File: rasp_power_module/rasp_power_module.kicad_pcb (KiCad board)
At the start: 2 copper layers, 45.7 x 59.3 mm, 22 parts, among them J1 Conn_01x02, J2 Conn_01x05, J3 Conn_01x02, J5 Conn_01x02, J7 Conn_01x02, J8 Conn_01x02, J9 Conn_01x02, K1 G5V-1, K2 SANYOU_SRD_Form_C, Q1 S8050 J3Y

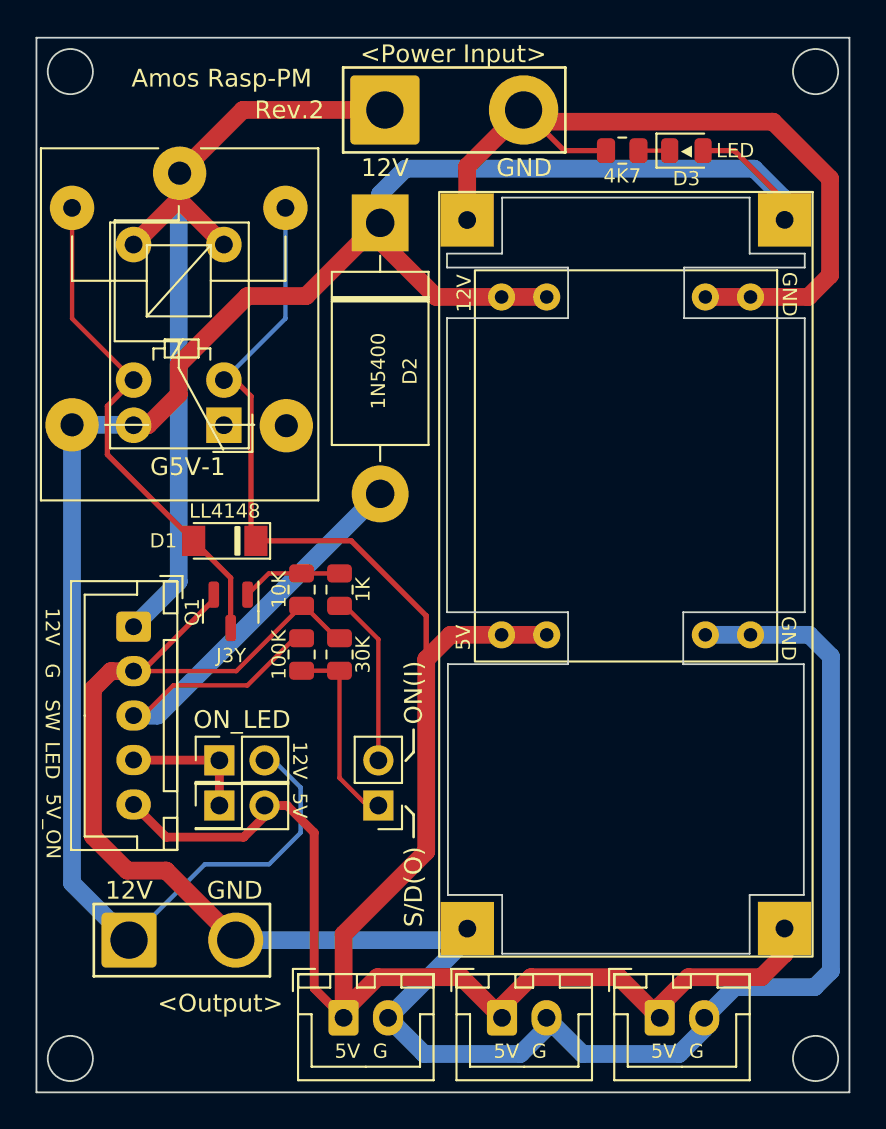
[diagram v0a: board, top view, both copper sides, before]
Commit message: rev.3  - mp1584 보드 핀아웃 조정
Signed-off-by: Ju, Gyeong-min <jcmh74@gmail.com>
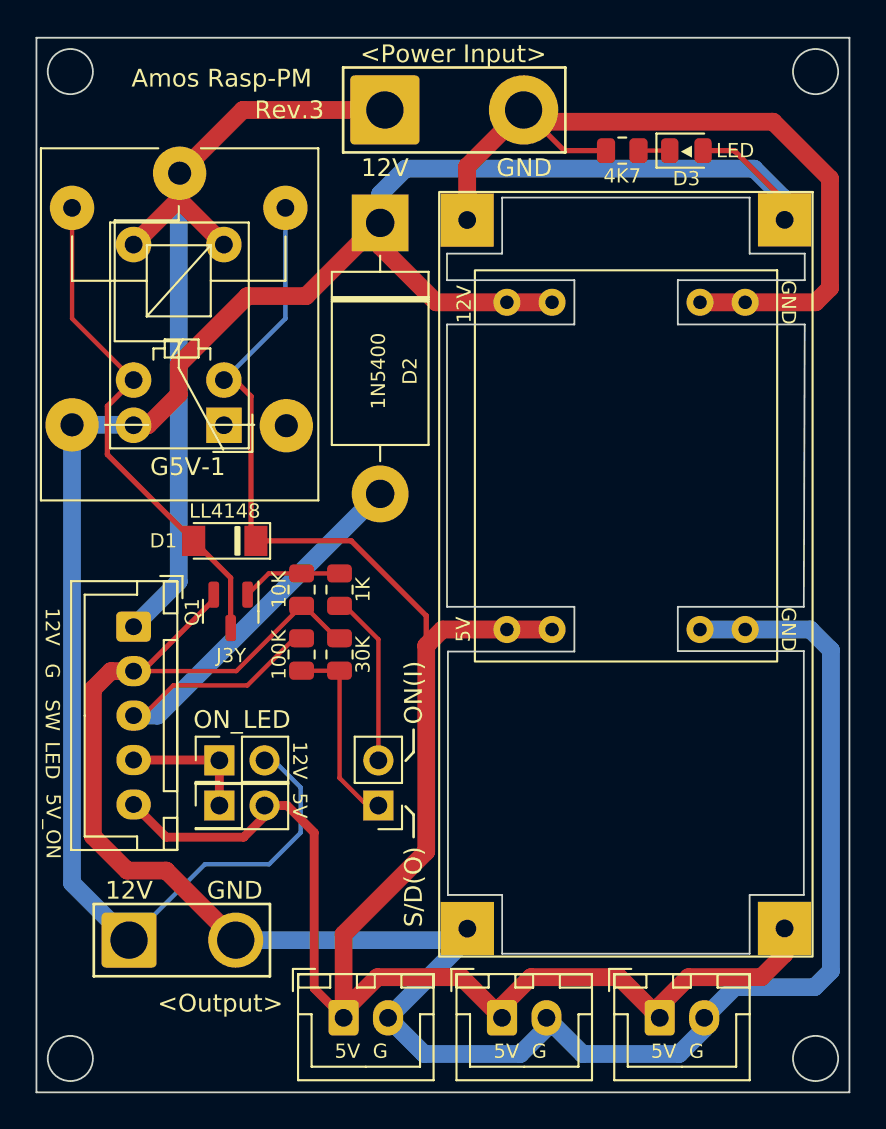
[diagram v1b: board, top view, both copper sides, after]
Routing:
- net InGND: track 162.1 -> 163.6 mm
- net 12V_ON: track 116.2 -> 116.8 mm
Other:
- outline, holes or cut-outs redrawn
- board text added: "Rev.3"
- board text removed: "Rev.2"

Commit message: PCB Rev 4 (안쪽 커팅라인 없앰)
Signed-off-by: Ju, Gyeong-min <jcmh74@gmail.com>
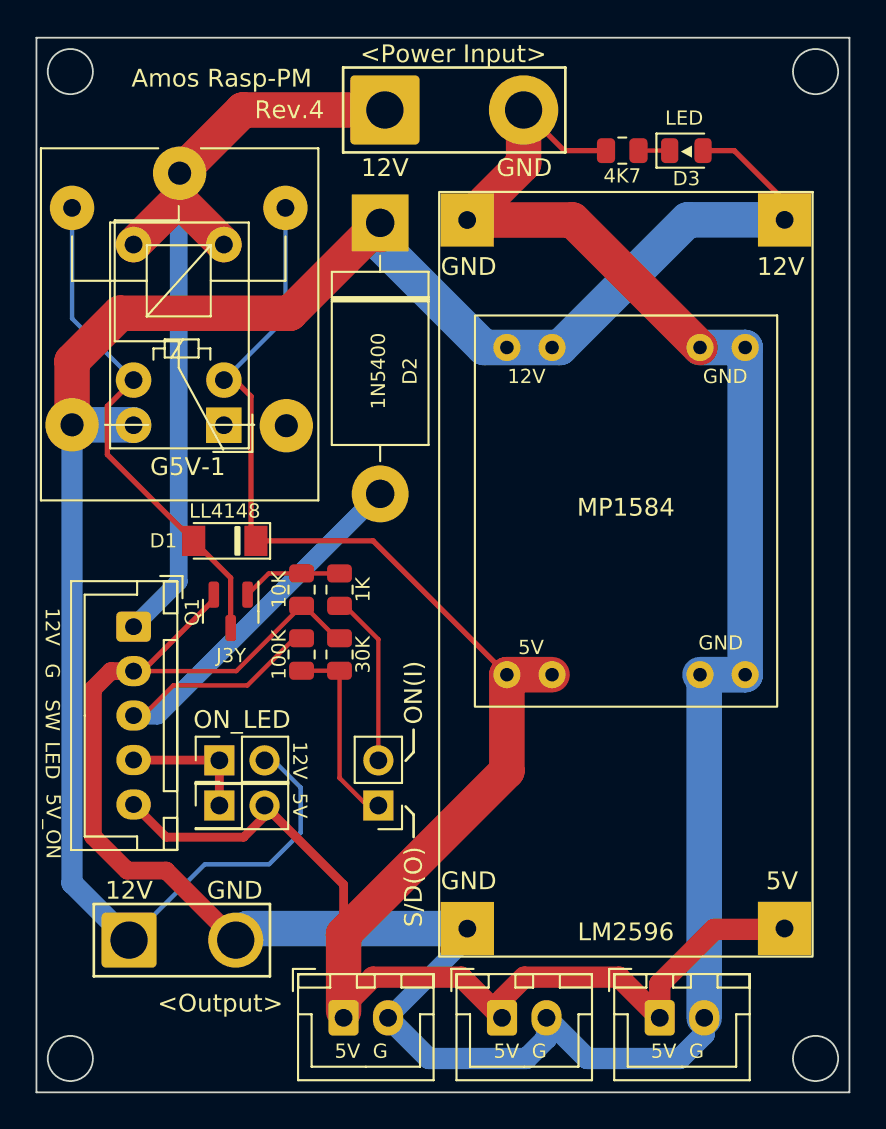
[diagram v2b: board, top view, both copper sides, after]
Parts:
- moved DCDC1 2.54 mm to (163.4, 73.0)
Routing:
- net InGND: track 163.6 -> 156.7 mm
- net 12V_ON: track 116.8 -> 112.3 mm
- net 5V_ON: track 120.4 -> 119.5 mm
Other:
- outline, holes or cut-outs redrawn
- board text added: "MP1584 Out"
- board text added: "Rev.4"
- board text removed: "Rev.3"
- board text removed: "◄MP1584 Out"

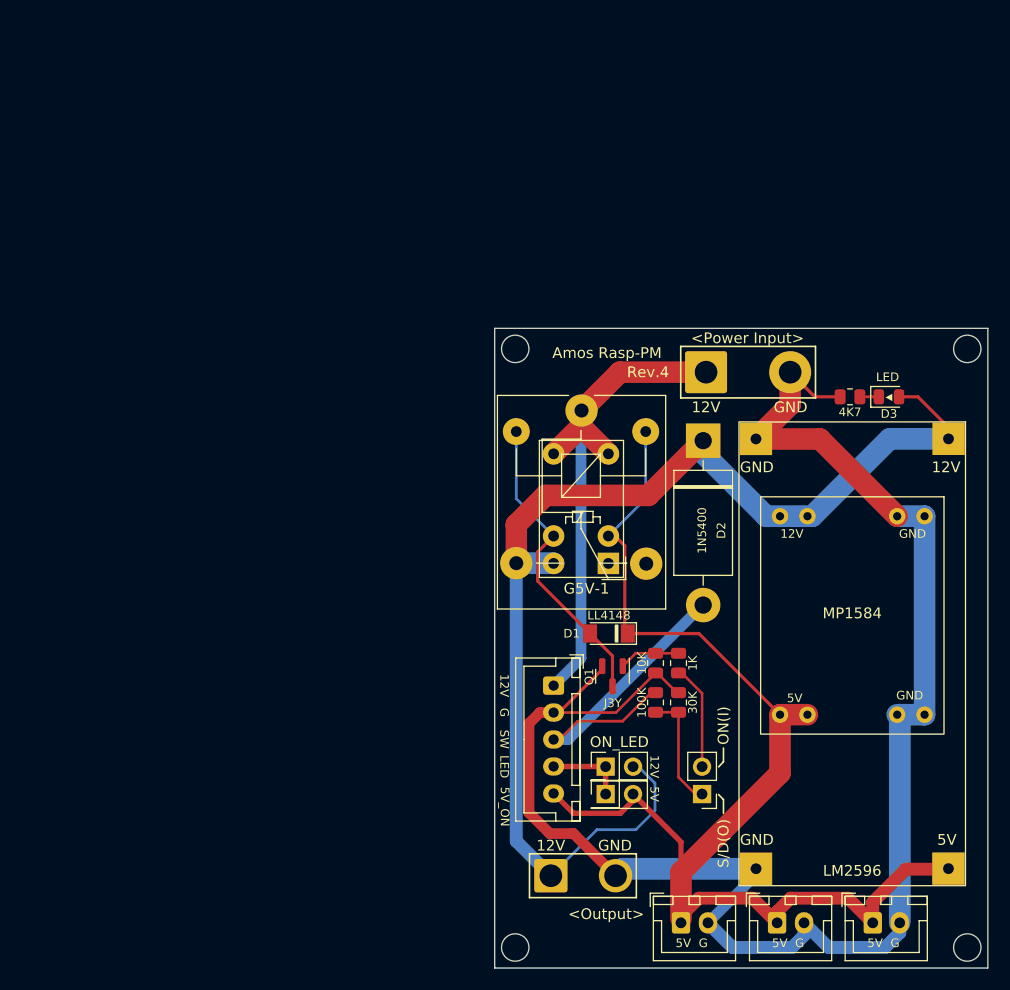
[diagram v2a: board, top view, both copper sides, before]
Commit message: MP8289 모듈 추가. Rev5
Signed-off-by: Ju, Gyeong-min <jcmh74@gmail.com>
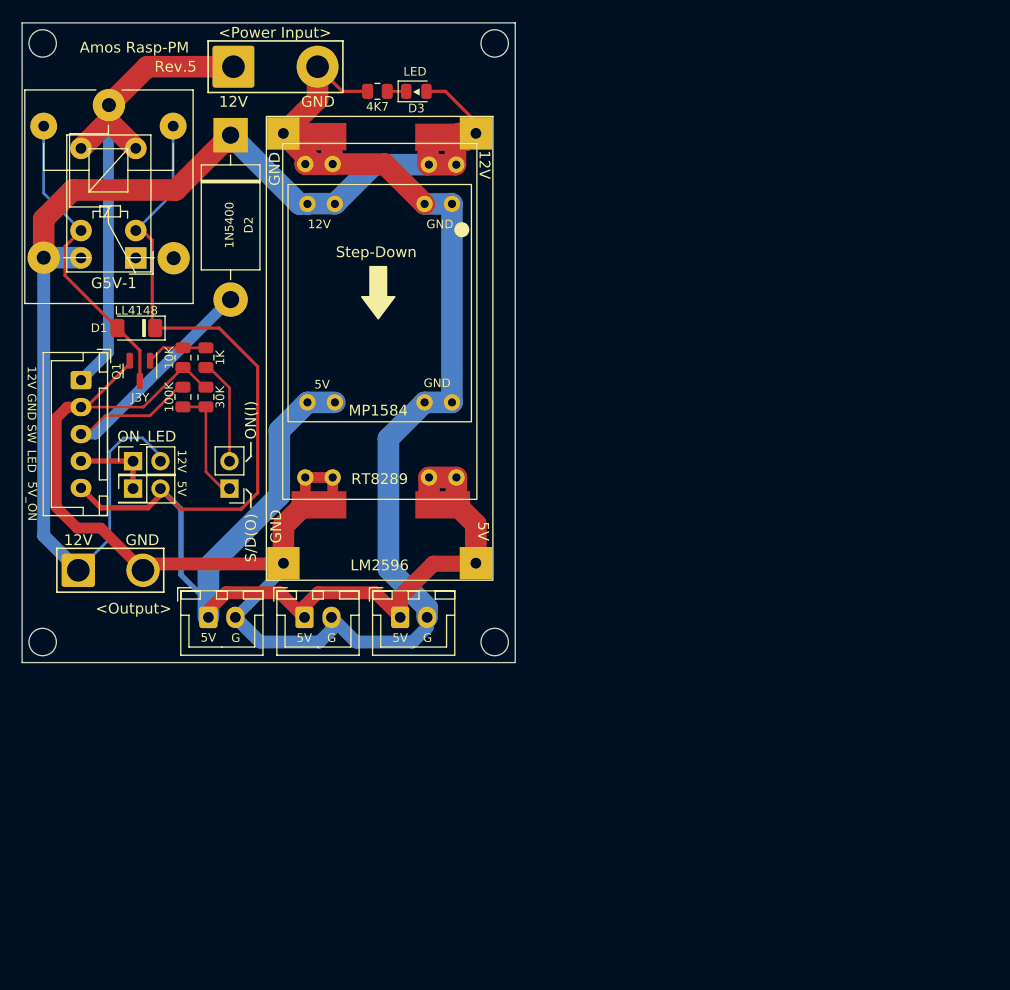
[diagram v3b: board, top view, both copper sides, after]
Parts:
- added DCDC3: RT8289_module, rasp_power_module:RT8289_dcdc_module, F.Cu at (120.1, 40.3)
- moved DCDC1 52.5 mm to (119.6, 44.1)
- moved D1 52.2 mm to (88.6, 57.4)
- moved D3 52.2 mm to (114.5, 35.4)
- moved J1 52.2 mm to (97.6, 33.1)
- moved J2 52.2 mm to (83.4, 62.2)
- moved J3 52.2 mm to (97.2, 72.3)
- moved JP1 52.2 mm to (88.3, 69.7)
- moved JP2 52.2 mm to (88.3, 72.3)
- moved J7 52.2 mm to (95.2, 84.2)
- moved J8 52.2 mm to (104.2, 84.2)
- moved J9 52.2 mm to (113.0, 84.2)
- moved Q1 52.2 mm to (88.9, 61.3)
- moved R1 52.2 mm to (95.0, 60.1)
- moved R2 52.2 mm to (92.9, 60.1)
- moved R3 52.2 mm to (92.9, 63.8)
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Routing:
- net 5V_ON: track 119.5 -> 149.8 mm
- net InGND: track 156.7 -> 183.4 mm
- net 12V_ON: track 112.3 -> 116.4 mm
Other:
- board text added: "RT8289"
- board text added: "Rev.5"
- board text added: "Step-Down"
- board text removed: "5V G"
- board text removed: "G 5V"
- board text removed: "In_GND"
- board text removed: "In_VCC"
- board text removed: "MP1584 Out"
- board text removed: "Out_GND"
- board text removed: "Out_VCC"
- board text removed: "Rev.4"
